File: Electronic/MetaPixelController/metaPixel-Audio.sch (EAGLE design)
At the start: 3 parts, among them IC1 74HC245N

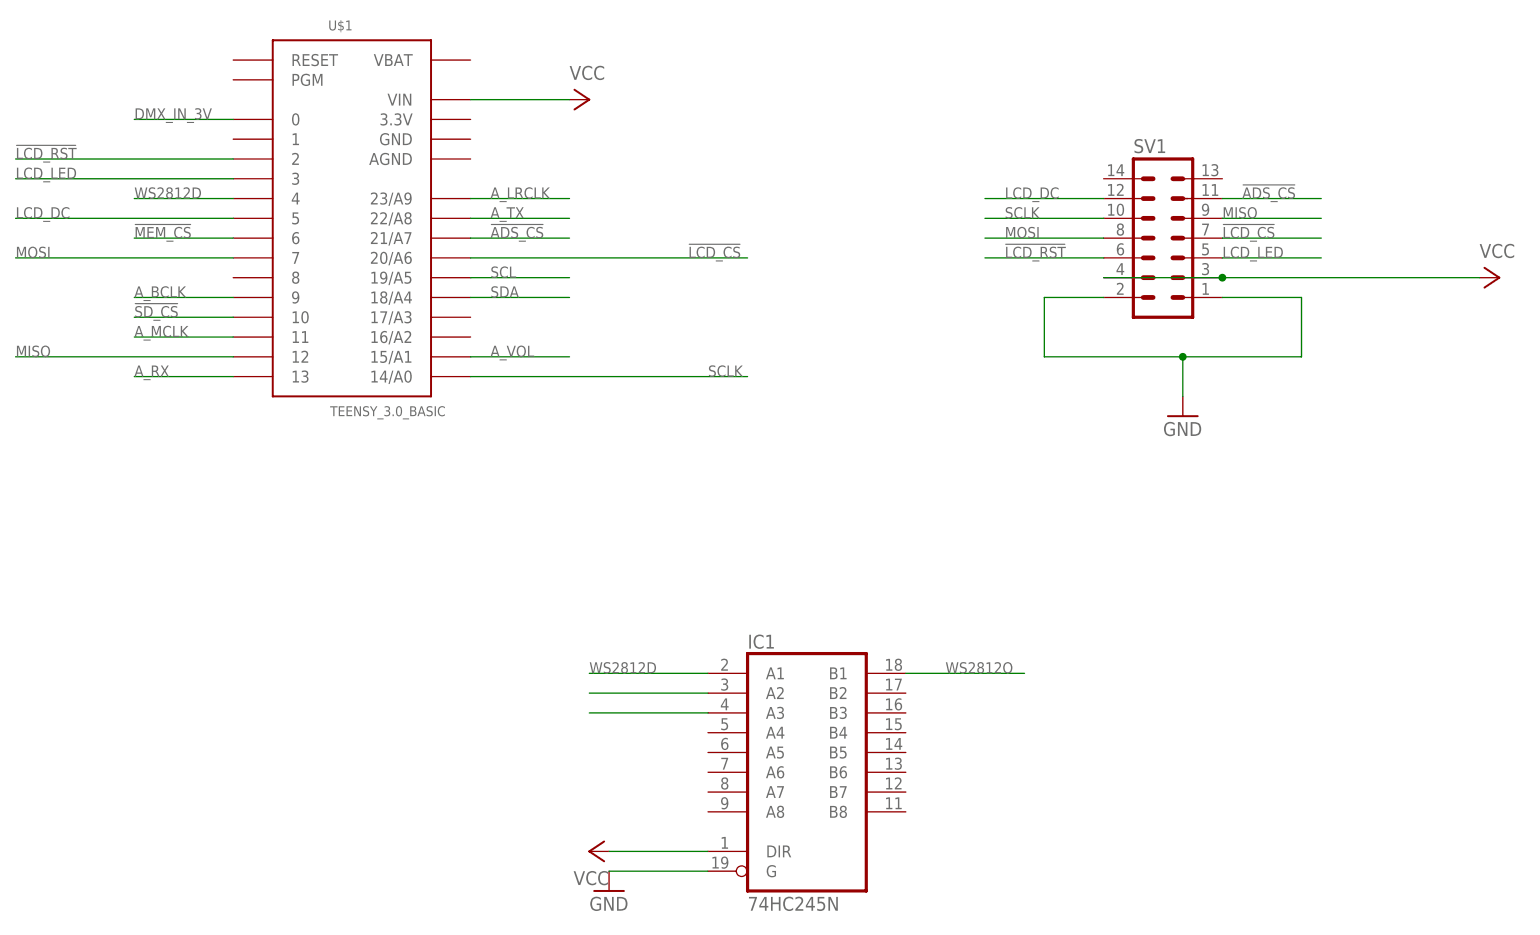
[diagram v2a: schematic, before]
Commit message: Added an ILI9341 Display
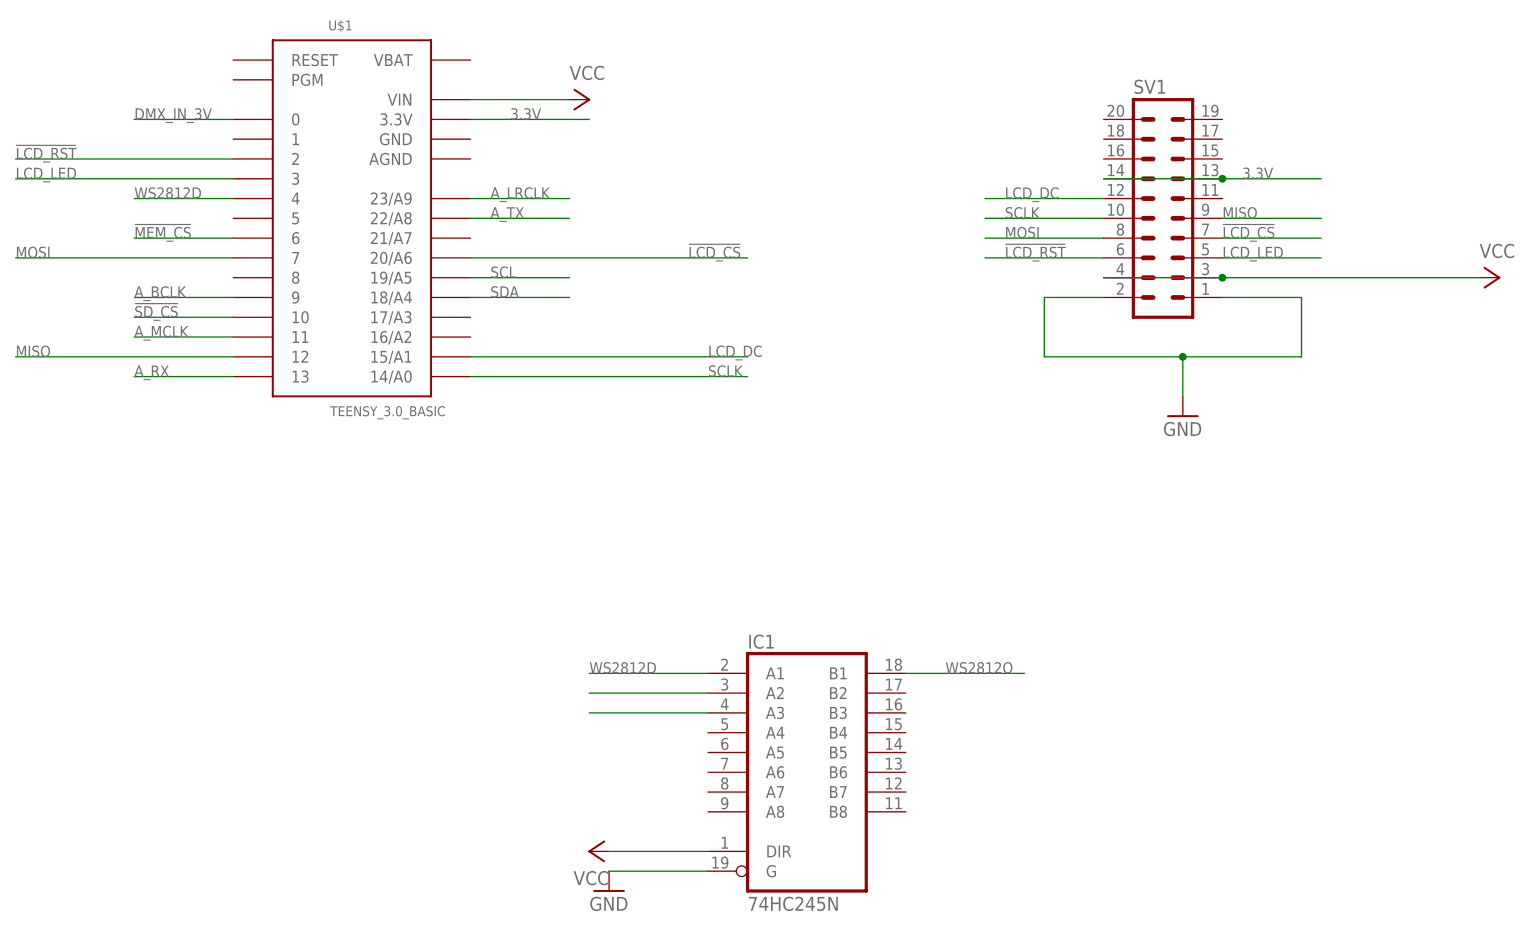
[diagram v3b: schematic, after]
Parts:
- SV1: device con-harting-ml:ML14 -> con-ml:ML20
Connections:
- removed net !ADS_CS: SV1.11, U$1.21/A7
- removed net A_VOL: U$1.15/A1
- new net 3.3V: SV1.13, SV1.14, U$1.3.3V
- net LCD_DC: now also U$1.15/A1; no longer U$1.5
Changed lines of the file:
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@@
 <?xml version="1.0" encoding="utf-8"?>
 <!DOCTYPE eagle SYSTEM "eagle.dtd">
-<eagle version="7.2.0">
+<eagle version="7.4.0">
 <drawing>
 <settings>
@@
 <layers>
 <layer number="1" name="Top" color="4" fill="1" visible="no" active="no"/>
+<layer number="2" name="Route2" color="1" fill="3" visible="no" active="no"/>
+<layer number="15" name="Route15" color="4" fill="6" visible="no" active="no"/>
 <layer number="16" name="Bottom" color="1" fill="1" visible="no" active="no"/>
 <layer number="17" name="Pads" color="2" fill="1" visible="no" active="no"/>
@@
 <part name="U$1" library="Teensy3.0" deviceset="TEENSY_3.0_BASIC" device=""/>
 <part name="GND1" library="supply1" deviceset="GND" device=""/>
-<part name="P+1" library="supply1" deviceset="VCC" device=""/>
+<part name="P+1" library="supply1" deviceset="VCC" device="" value="VCC"/>
 <part name="P+2" library="supply1" deviceset="VCC" device=""/>
-<part name="SV1" library="con-harting-ml" deviceset="ML14" device=""/>
 <part name="IC1" library="74xx-eu" deviceset="74*245" device="N" technology="HC"/>
 <part name="P+3" library="supply1" deviceset="VCC" device=""/>
 <part name="GND2" library="supply1" deviceset="GND" device=""/>
+<part name="SV1" library="con-ml" deviceset="ML20" device=""/>
 </parts>
 <sheets>
@@
 <instance part="P+1" gate="VCC" x="185.42" y="35.56" rot="R270"/>
 <instance part="P+2" gate="VCC" x="68.58" y="58.42" rot="R270"/>
-<instance part="SV1" gate="1" x="142.24" y="40.64"/>
 <instance part="IC1" gate="A" x="96.52" y="-27.94"/>
 <instance part="P+3" gate="VCC" x="68.58" y="-38.1" rot="R90"/>
 <instance part="GND2" gate="1" x="71.12" y="-43.18"/>
+<instance part="SV1" gate="1" x="142.24" y="45.72"/>
 </instances>
 <busses>
@@
 <wire x1="53.34" y1="45.72" x2="66.04" y2="45.72" width="0.1524" layer="91"/>
 <label x="55.88" y="45.72" size="1.4224" layer="95"/>
-</segment>
-</net>
-<net name="A_VOL" class="0">
-<segment>
-<pinref part="U$1" gate="G$1" pin="15/A1"/>
-<wire x1="53.34" y1="25.4" x2="66.04" y2="25.4" width="0.1524" layer="91"/>
-<label x="55.88" y="25.4" size="1.4224" layer="95"/>
 </segment>
 </net>
@@
 <net name="VCC" class="0">
 <segment>
+<pinref part="U$1" gate="G$1" pin="VIN"/>
+<wire x1="53.34" y1="58.42" x2="66.04" y2="58.42" width="0.1524" layer="91"/>
+<pinref part="P+2" gate="VCC" pin="VCC"/>
+</segment>
+<segment>
+<pinref part="IC1" gate="A" pin="DIR"/>
+<wire x1="83.82" y1="-38.1" x2="71.12" y2="-38.1" width="0.1524" layer="91"/>
+<pinref part="P+3" gate="VCC" pin="VCC"/>
+</segment>
+<segment>
+<pinref part="P+1" gate="VCC" pin="VCC"/>
 <wire x1="134.62" y1="35.56" x2="149.86" y2="35.56" width="0.1524" layer="91"/>
-<pinref part="P+1" gate="VCC" pin="VCC"/>
 <pinref part="SV1" gate="1" pin="3"/>
 <wire x1="149.86" y1="35.56" x2="182.88" y2="35.56" width="0.1524" layer="91"/>
@@
 <pinref part="SV1" gate="1" pin="4"/>
 </segment>
-<segment>
-<pinref part="U$1" gate="G$1" pin="VIN"/>
-<wire x1="53.34" y1="58.42" x2="66.04" y2="58.42" width="0.1524" layer="91"/>
-<pinref part="P+2" gate="VCC" pin="VCC"/>
-</segment>
-<segment>
-<pinref part="IC1" gate="A" pin="DIR"/>
-<wire x1="83.82" y1="-38.1" x2="71.12" y2="-38.1" width="0.1524" layer="91"/>
-<pinref part="P+3" gate="VCC" pin="VCC"/>
-</segment>
 </net>
 <net name="LCD_LED" class="0">
@@
 </segment>
 </net>
-<net name="!ADS_CS" class="0">
-<segment>
-<wire x1="149.86" y1="45.72" x2="162.56" y2="45.72" width="0.1524" layer="91"/>
-<label x="152.4" y="45.72" size="1.4224" layer="95"/>
-<pinref part="SV1" gate="1" pin="11"/>
-</segment>
-<segment>
-<pinref part="U$1" gate="G$1" pin="21/A7"/>
-<wire x1="53.34" y1="40.64" x2="66.04" y2="40.64" width="0.1524" layer="91"/>
-<label x="55.88" y="40.64" size="1.4224" layer="95"/>
-</segment>
-</net>
 <net name="DMX_IN_3V" class="0">
 <segment>
@@
 <net name="LCD_DC" class="0">
 <segment>
-<pinref part="SV1" gate="1" pin="12"/>
 <wire x1="134.62" y1="45.72" x2="119.38" y2="45.72" width="0.1524" layer="91"/>
 <label x="121.92" y="45.72" size="1.4224" layer="95"/>
-</segment>
-<segment>
-<pinref part="U$1" gate="G$1" pin="5"/>
-<wire x1="22.86" y1="43.18" x2="-5.08" y2="43.18" width="0.1524" layer="91"/>
-<label x="-5.08" y="43.18" size="1.4224" layer="95"/>
-</segment>
-</net>
+<pinref part="SV1" gate="1" pin="12"/>
+</segment>
+<segment>
+<pinref part="U$1" gate="G$1" pin="15/A1"/>
+<wire x1="53.34" y1="25.4" x2="88.9" y2="25.4" width="0.1524" layer="91"/>
+<label x="83.82" y="25.4" size="1.4224" layer="95"/>
+</segment>
+</net>
+<net name="3.3V" class="0">
+<segment>
+<pinref part="U$1" gate="G$1" pin="3.3V"/>
+<wire x1="53.34" y1="55.88" x2="68.58" y2="55.88" width="0.1524" layer="91"/>
+<label x="58.42" y="55.88" size="1.4224" layer="95"/>
+</segment>
+<segment>
+<wire x1="134.62" y1="48.26" x2="149.86" y2="48.26" width="0.1524" layer="91"/>
+<label x="152.4" y="48.26" size="1.4224" layer="95"/>
+<pinref part="SV1" gate="1" pin="13"/>
+<wire x1="149.86" y1="48.26" x2="162.56" y2="48.26" width="0.1524" layer="91"/>
+<junction x="149.86" y="48.26"/>
+<pinref part="SV1" gate="1" pin="14"/>
+</segment>
+</net>
